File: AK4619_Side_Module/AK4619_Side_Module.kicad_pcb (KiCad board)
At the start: 4 copper layers, 40 x 87 mm, 58 parts, among them J1 Conn_01x02, J2 AudioJack2_Ground, J3 AudioJack2_Ground, J4 Conn_01x11, J5 AudioJack2_Ground, J6 AudioJack2_Ground, SW1 SKRPABE010, U1 AP7361EA-33E-13, U2 AK4619VN, U3 ADM811TARTZ

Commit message: Add dimension annotations to the PCB data.
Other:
- board text added: "UNIT: mm t: 1.6"

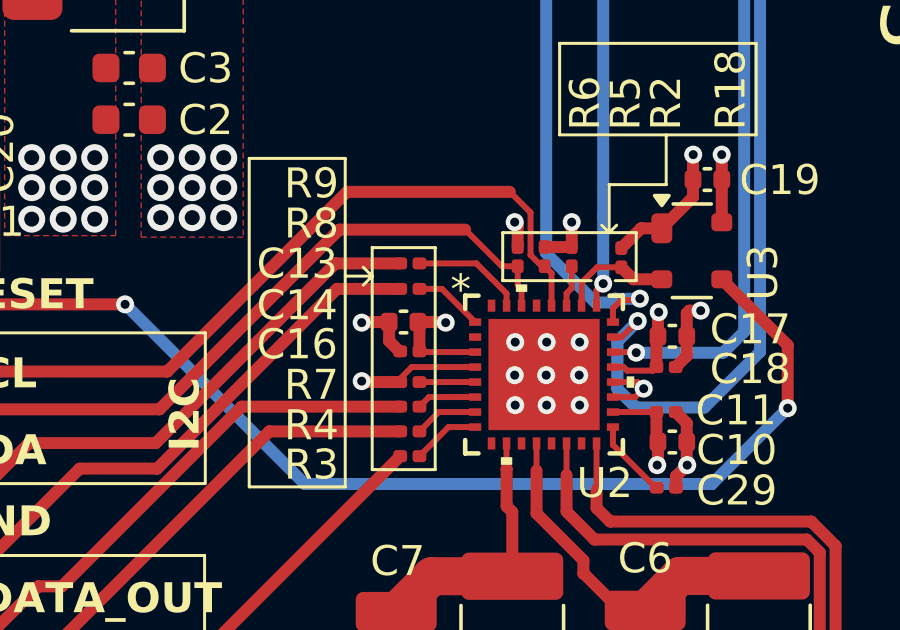
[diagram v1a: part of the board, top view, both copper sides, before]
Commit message: Change the 3D model data path settings.
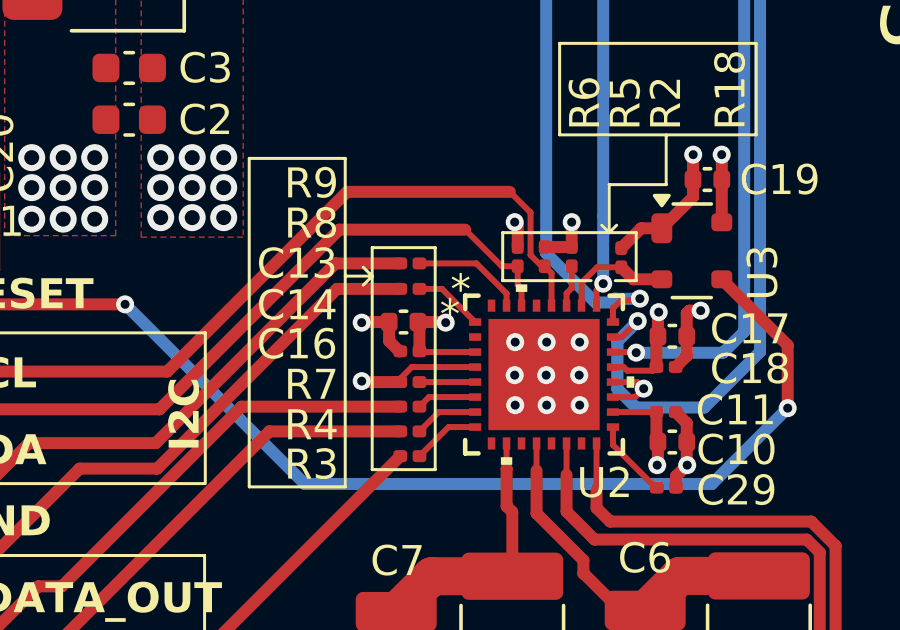
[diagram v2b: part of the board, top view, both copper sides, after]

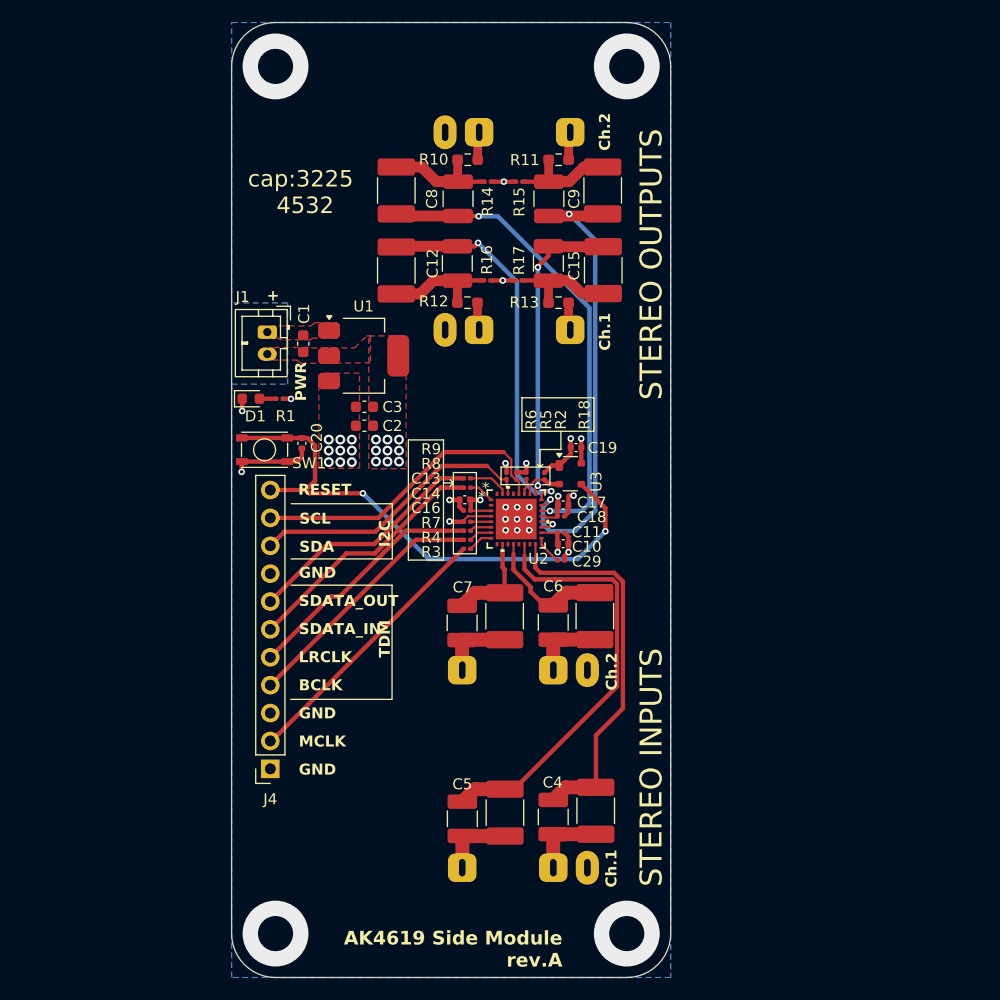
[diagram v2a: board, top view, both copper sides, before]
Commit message: Add dimension annotations
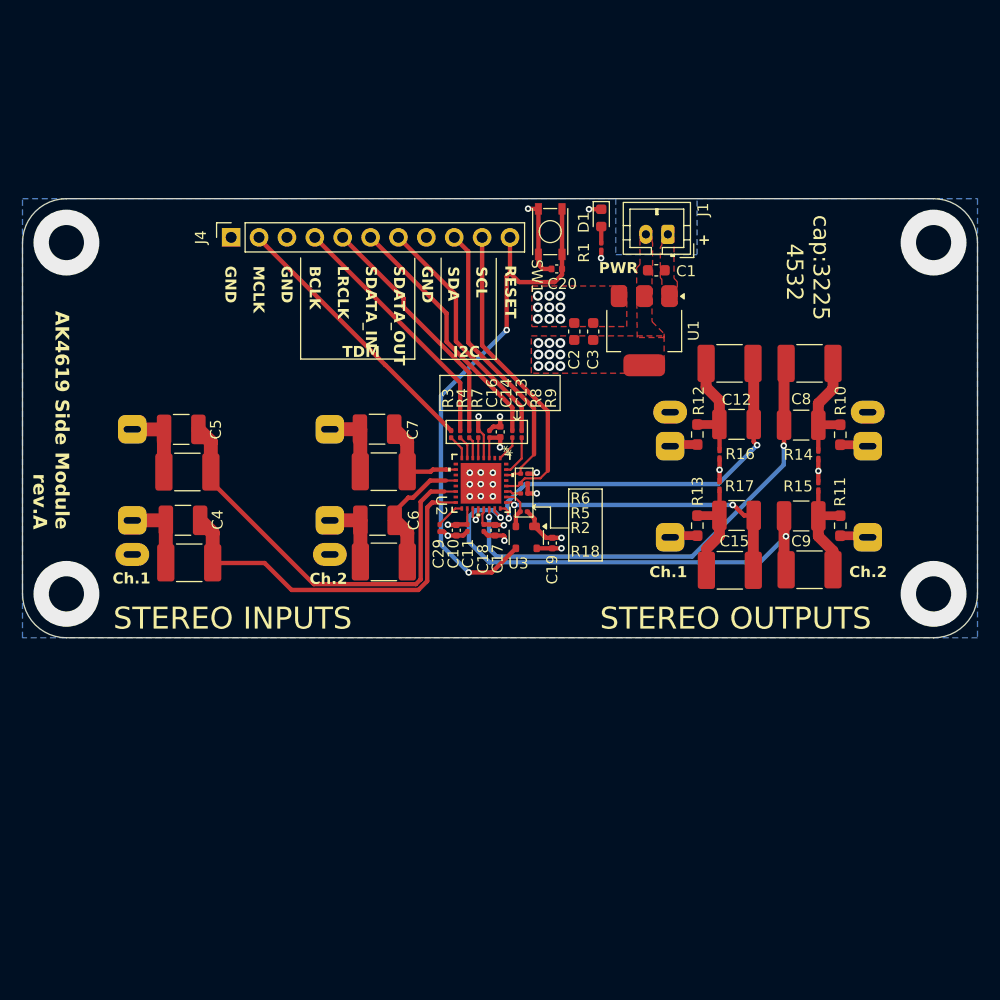
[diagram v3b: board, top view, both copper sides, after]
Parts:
- moved J2 49.5 mm to (118.7, 94.0), turned to 180 degrees
- moved J4 48.5 mm to (127.7, 71.6), turned to 90 degrees
- moved J5 45.3 mm to (185.7, 94.0), turned to 0 degrees
- moved C5 43.7 mm to (123.2, 89.1), turned to 180 degrees
- moved C21 43.4 mm to (123.9, 101.2), turned to 180 degrees
- moved C4 43.2 mm to (123.3, 97.3), turned to 180 degrees
- moved C22 42.4 mm to (123.7, 93.0), turned to 180 degrees
- moved R10 42.2 mm to (183.2, 89.6), turned to -90 degrees
- moved R11 42.1 mm to (183.2, 97.8), turned to -90 degrees
- moved C25 40.8 mm to (180.4, 83.1), turned to 0 degrees
- moved C26 39.4 mm to (180.4, 101.9), turned to 0 degrees
- moved R14 39.1 mm to (181.2, 91.4), turned to 90 degrees
- moved R15 38.9 mm to (181.2, 94.3), turned to -90 degrees
- moved J1 37.6 mm to (167.5, 71.3), turned to 180 degrees
- moved C8 37.4 mm to (179.6, 88.7), turned to 0 degrees
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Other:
- board size 40 x 87 mm -> 87 x 40 mm
